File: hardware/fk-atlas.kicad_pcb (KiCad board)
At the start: 4 copper layers, 88.4 x 80.3 mm, 143 parts, among them J1 CONN_02x05_SWD, J10 CONN_01x04, J2 MICRO-USB-VERT-TOP, J201 CONN_01X02, J3 CONN_01x02, J301 CONN_01X02, J4 CONN_01x03_SERIAL, J401 CONN_01X02, J5 CONN_01x05, J501 CONN_01X02, J6 CONN_01x04, J601 CONN_01X02, J7 CONN_01x05, J8 CONN_01x02, J9 MICRO-USB-HORIZ-BOTTOM, M1 MOUNT_HOLE, M2 MOUNT_HOLE, M3 MOUNT_HOLE, M4 MOUNT_HOLE, M5 FIDUCIAL, M6 FIDUCIAL, M7 FIDUCIAL, P2 ATLAS_EC_PROBE, P3 ATLAS_RTD_PROBE, P4 ATLAS_PH_PROBE, P5 ATLAS_DO_PROBE, P6 ATLAS_ORP_PROBE, Q4 2N7002LT1G, SW1 SPNO, U1 S25FL116K0XMFI041, U2 ATSAMD21G18A-AU, U201 ADM3260, U202 ATLAS_EC, U3 MCP1700T-3302E/MB, U301 ADM3260, U302 ATLAS_RTD, U4 TPS2052B, U401 ADM3260, U402 ATLAS_PH, U5 SK6812, U501 ADM3260, U502 ATLAS_DO, U601 ADM3260, U602 ATLAS_ORP, Y1 FC-135

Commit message: Finished DRC check, no errors
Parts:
- added C22: 10uF, conservify:CAP-0603, F.Cu at (132.6, 119.0)
- added C23: 10uF, conservify:CAP-0603, F.Cu at (134.1, 119.0)
- added C24: 100nF, conservify:CAP-0603, F.Cu at (125.5, 132.2)
- added G***: LOGO, conservify:LOGO_CONSERVIFY_TEXT_NEGATIVE_4000, F.Cu at (136.0, 80.3)
- added G***: LOGO, conservify:LOGO_FK_NEGATIVE_2500, F.Cu at (141.1, 82.4)
- added G***: LOGO, conservify:LOGO_OSH_NEGATIVE_3000, F.Cu at (145.3, 135.0)
- J10: footprint conservify:Molex_CLIK-Mate_502382-0470_1x04_P1.25mm_Vertical -> conservify:BM04B-SRSS-TB
- R13, R14: value ? -> 100K
- moved R14 47.5 mm to (141.9, 124.2), turned to 270 degrees
- moved C606 6.17 mm to (187.2, 132.6), turned to 90 degrees
- moved C506 6.10 mm to (187.3, 116.7), turned to 90 degrees
- moved C18 4.85 mm to (143.4, 124.2)
- moved R12 4.32 mm to (137.0, 126.2)
- moved C19 3.89 mm to (140.5, 124.2)
- moved J10 3.19 mm to (126.6, 127.3)
- moved C406 1.05 mm to (187.5, 100.8)
- moved C306 0.79 mm to (187.5, 85.3), turned to 90 degrees
- moved C206 0.57 mm to (187.5, 68.8)
- moved R7 0.28 mm to (138.9, 124.2)
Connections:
- J10 pad 1: Net-(J10-Pad1) -> GND
- J10 pad 2: Net-(J10-Pad2) -> 3V3
- J10 pad 3: Net-(J10-Pad3) -> /SDA2
- J10 pad 4: Net-(J10-Pad4) -> /SCL2
- J5 pad 3: VIN -> Net-(J5-Pad3)
- J7 pad 3: VIN -> Net-(J7-Pad3)
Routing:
- net VCC: track 29.4 -> 50.0 mm, vias 6 -> 21
- net /PERIPH_3V3: track 40.9 -> 59.8 mm
- net /isolated_atlas2/ISO_SDA: track 20.5 -> 37.5 mm
- net /isolated_atlas3/ISO_SDA: track 20.4 -> 37.3 mm
- net Net-(J301-Pad2): track 11.8 -> 24.1 mm
- net /isolated_atlas1/ISO_VCC: track 12.5 -> 22.0 mm, vias 2 -> 4
- net /isolated_atlas2/ISO_VCC: track 13.0 -> 20.5 mm, vias 3 -> 4
- net /isolated_atlas0/ISO_VCC: track 14.3 -> 21.0 mm
- net GND: track 107.0 -> 100.7 mm, vias 61 -> 77
- net Net-(R12-Pad1): track 3.88 -> 9.76 mm, vias 0 -> 2
- net Net-(J401-Pad2): track 9.52 -> 15.0 mm
- net /isolated_atlas3/ISO_GND: track 7.87 -> 12.8 mm, vias 3 -> 8
- net /isolated_atlas2/ISO_SCL: track 20.3 -> 24.4 mm
- net /isolated_atlas3/ISO_SCL: track 20.3 -> 24.4 mm
- net 3V3: track 36.5 -> 32.4 mm, vias 25 -> 34
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- added copper zone on PWR, net /isolated_atlas3/ISO_VCC
- removed copper zone on PWR, net VIN

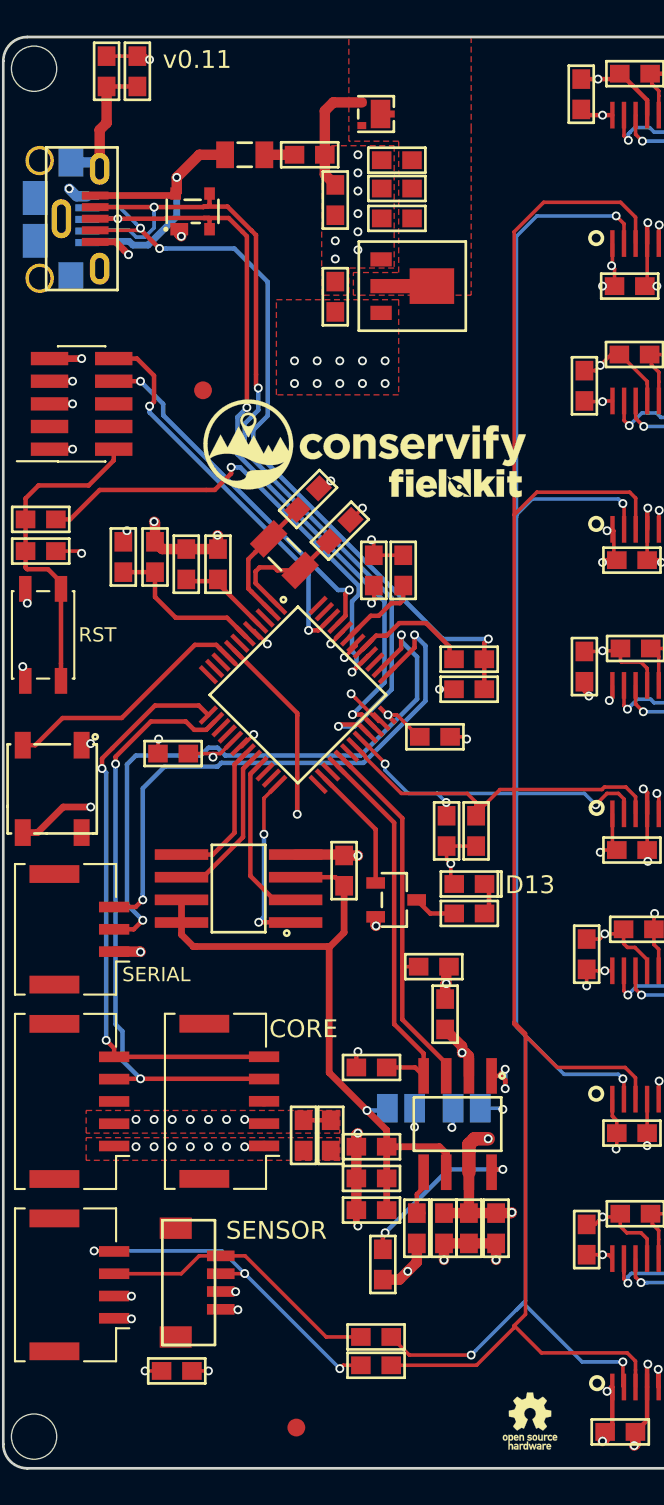
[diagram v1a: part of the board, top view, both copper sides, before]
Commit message: Added a power indicator LED, finished touching up traces and added logos, markings back in
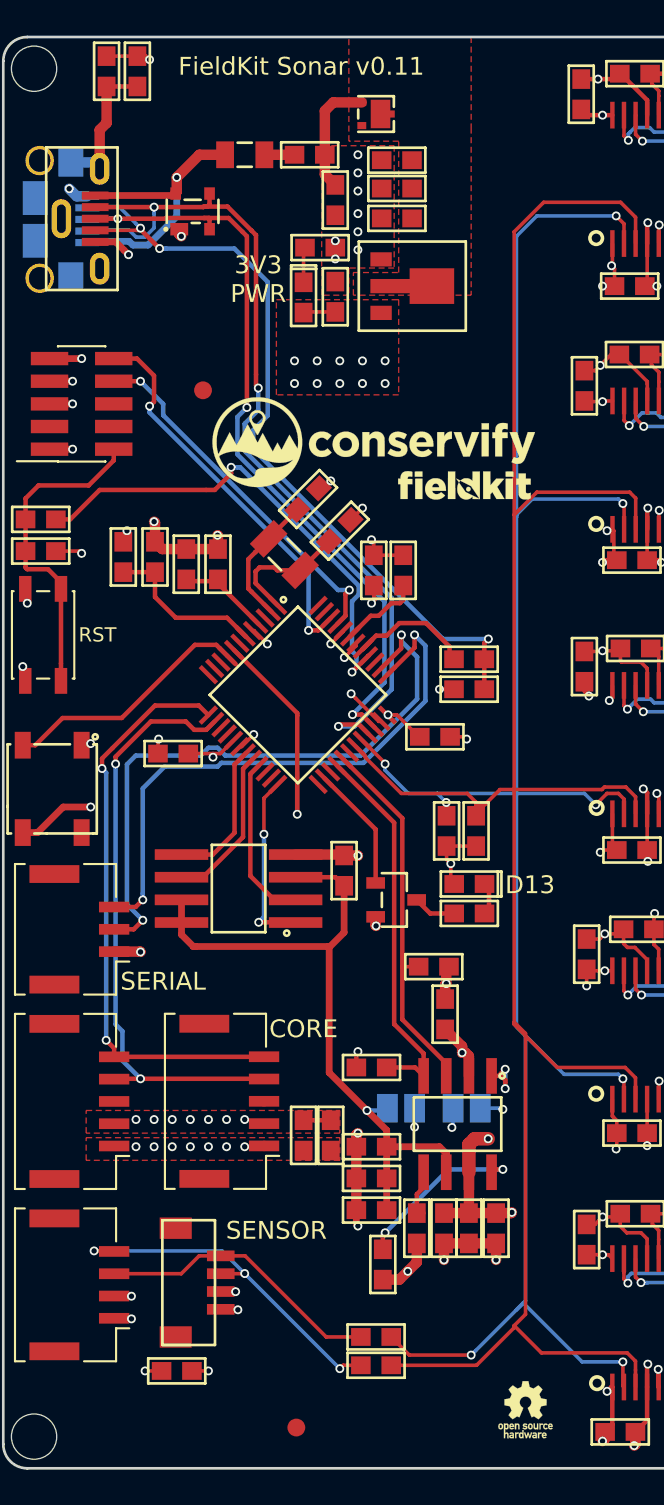
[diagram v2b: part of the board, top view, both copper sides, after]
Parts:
- added D1: Green, conservify:LED-0603, F.Cu at (132.6, 72.0)
- added R17: 2K2, conservify:RES-0603, F.Cu at (133.5, 69.2)
- moved G*** 0.68 mm to (145.0, 134.4)
- moved G*** 0.52 mm to (136.5, 80.1)
- moved G*** 0.52 mm to (141.6, 82.5)
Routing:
- net Net-(D1-Pad1): track 0.00 -> 1.98 mm
- net 3V3: track 32.4 -> 34.2 mm
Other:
- board text added: "3V3 PWR"
- board text added: "FieldKit Sonar v0.11"
- board text removed: "v0.11"

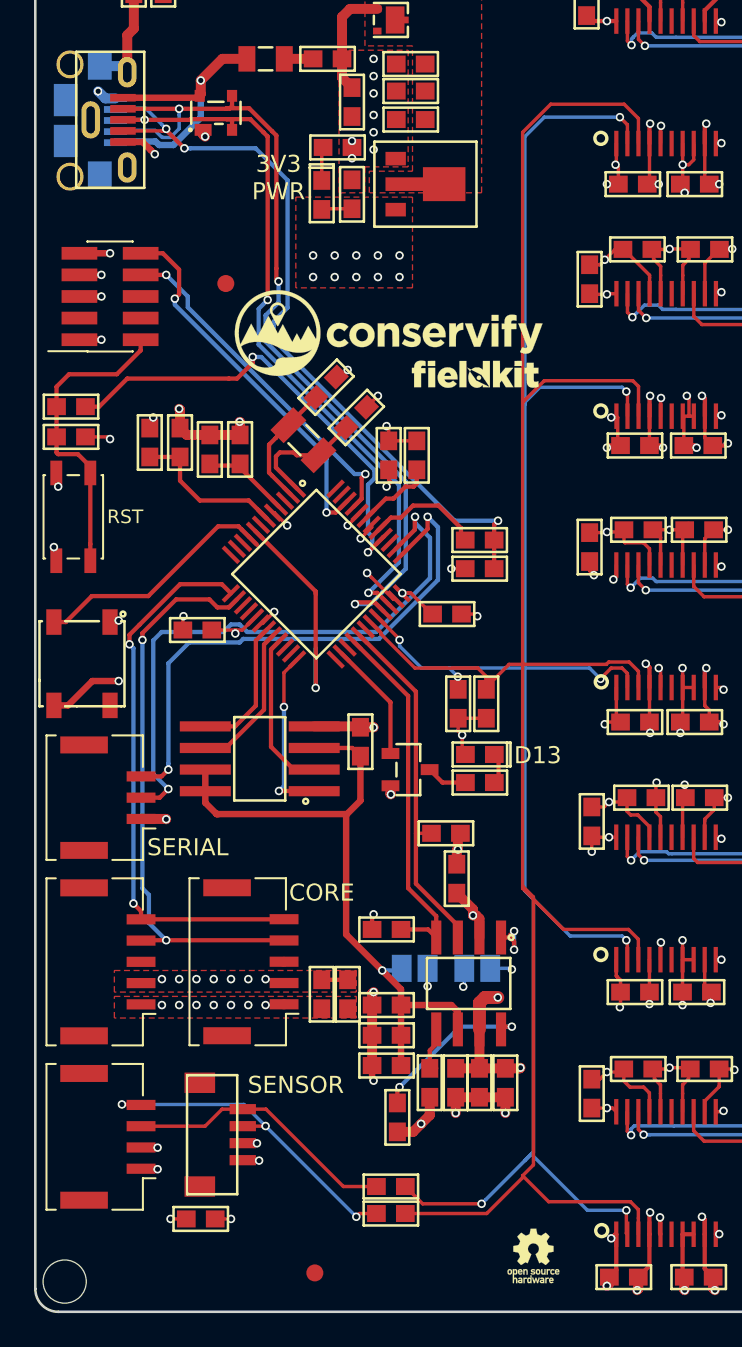
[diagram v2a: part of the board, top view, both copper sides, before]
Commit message: Added pull up resistors and a debounce cap for the reset button
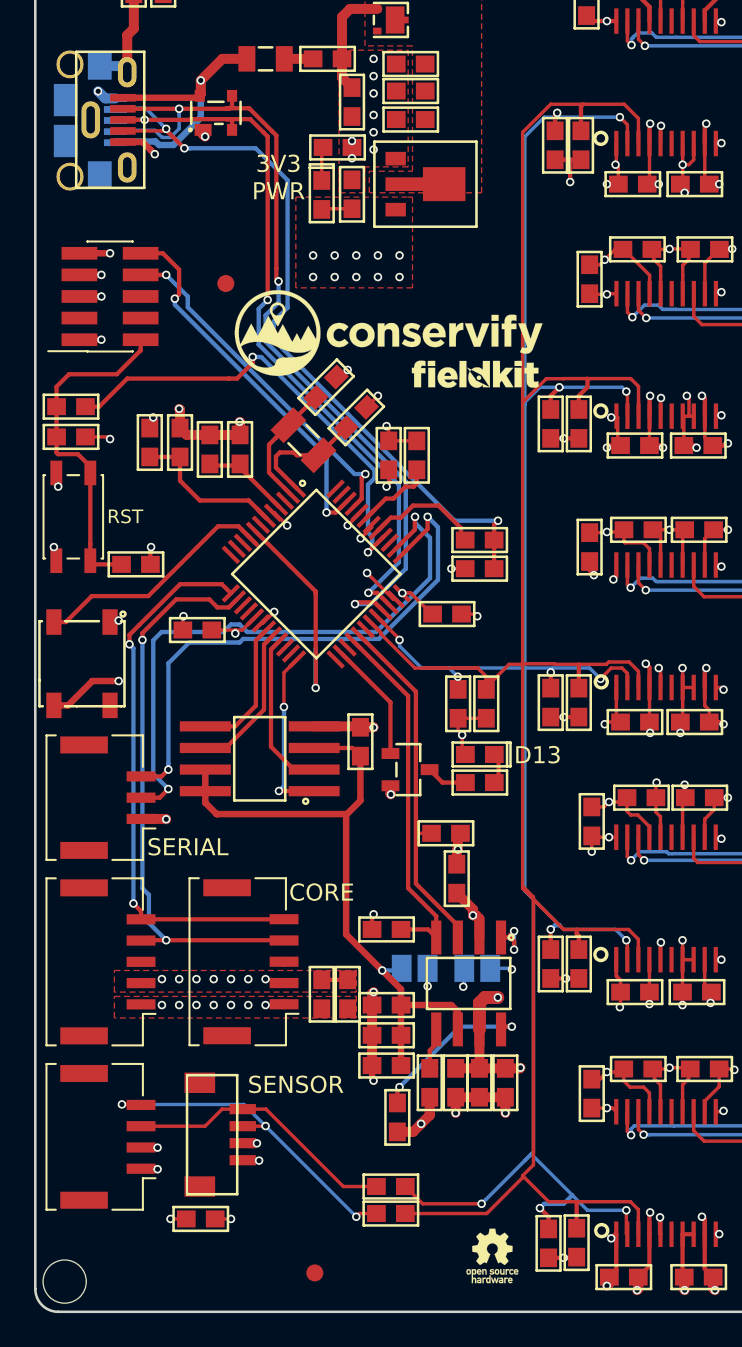
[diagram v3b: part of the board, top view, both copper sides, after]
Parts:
- added C25: 100nF, conservify:CAP-0603, F.Cu at (121.7, 93.7)
- added R18: 4.7K, conservify:RES-0603, F.Cu at (147.7, 117.2)
- added R19: 4.7K, conservify:RES-0603, F.Cu at (146.1, 117.2)
- added R20: 4.7K, conservify:RES-0603, F.Cu at (147.8, 69.1)
- added R21: 4.7K, conservify:RES-0603, F.Cu at (146.3, 69.1)
- added R22: 4.7K, conservify:RES-0603, F.Cu at (146.1, 85.5)
- added R23: 4.7K, conservify:RES-0603, F.Cu at (147.7, 85.5)
- added R24: 4.7K, conservify:RES-0603, F.Cu at (146.1, 101.9)
- added R25: 4.7K, conservify:RES-0603, F.Cu at (147.7, 101.9)
- added R26: 4.7K, conservify:RES-0603, F.Cu at (145.9, 133.6)
- added R27: 4.7K, conservify:RES-0603, F.Cu at (147.6, 133.6)
- moved G*** 2.41 mm to (142.6, 134.4)
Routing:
- net /SCL1: track 121.3 -> 130.9 mm, vias 8 -> 13
- net VCC: track 50.0 -> 59.5 mm, vias 21 -> 26
- net /SDA1: track 126.1 -> 134.1 mm
- net /RST: track 18.2 -> 20.1 mm
- net GND: track 100.7 -> 101.7 mm, vias 77 -> 78

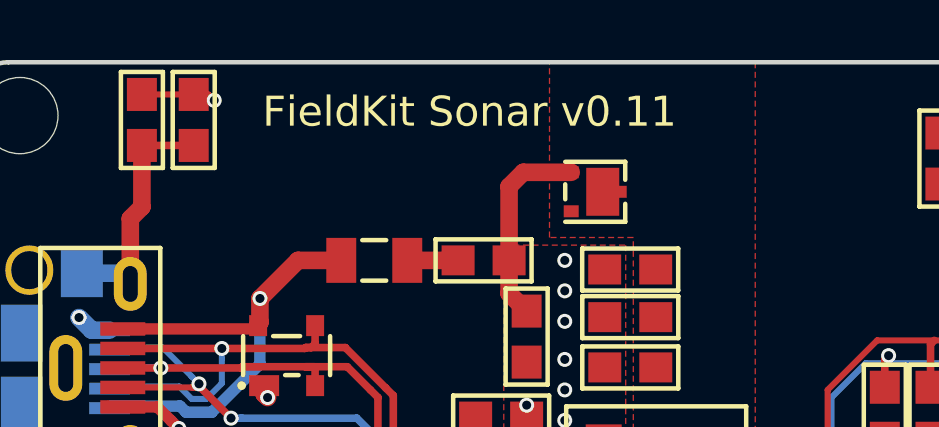
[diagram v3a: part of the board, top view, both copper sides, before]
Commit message: Fix board name on silk.
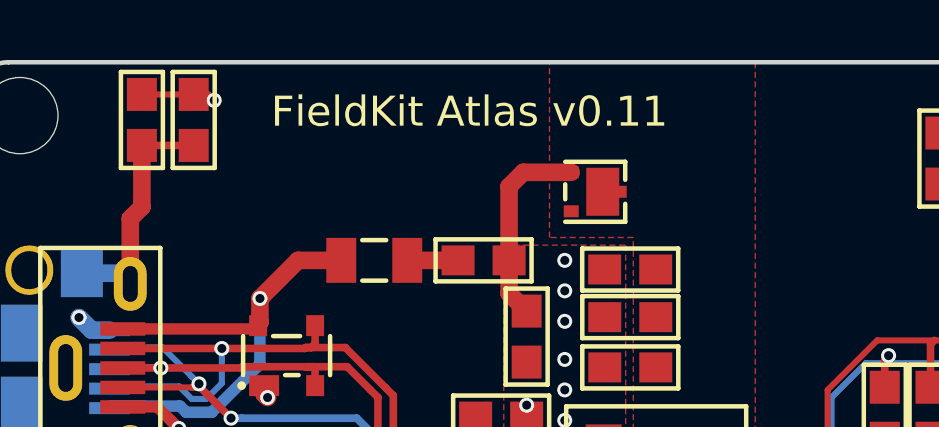
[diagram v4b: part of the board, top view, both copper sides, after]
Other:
- board text added: "FieldKit Atlas v0.11"
- board text removed: "FieldKit Sonar v0.11"
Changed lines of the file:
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@@
-(kicad_pcb (version 20171130) (host pcbnew "(5.0.0)")
+(kicad_pcb (version 20171130) (host pcbnew 5.0.1-33cea8e~67~ubuntu18.04.1)
   (general
     (thickness 1.6)
@@
     (effects (font (size 1.5 1.5) (thickness 0.25)))
   )
-  (gr_text "FieldKit Sonar v0.11" (at 132.461 59.055) (layer F.SilkS)
+  (gr_text "FieldKit Atlas v0.11" (at 132.461 59.055) (layer F.SilkS)
     (effects (font (size 1 1) (thickness 0.2)))
   )

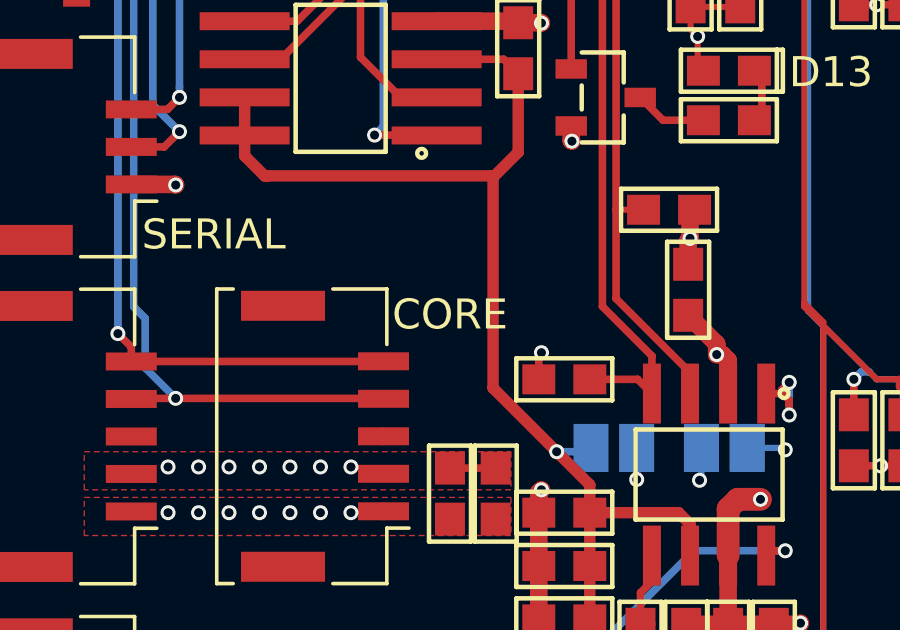
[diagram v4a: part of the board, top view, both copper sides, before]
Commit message: Generated panelized version of v0.11, including gerbers
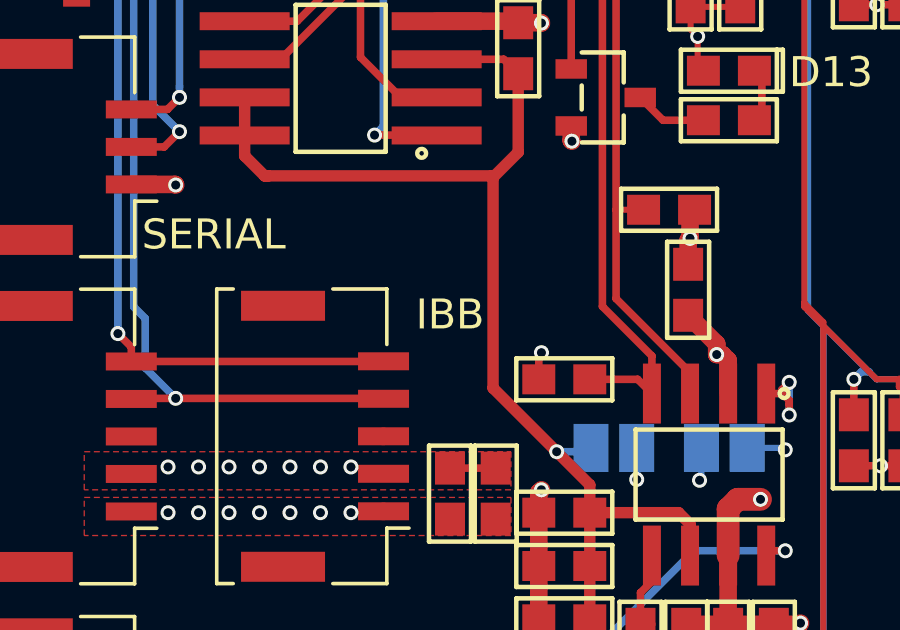
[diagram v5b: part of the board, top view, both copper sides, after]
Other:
- board text added: "IBB"
- board text removed: "CORE"
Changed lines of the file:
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@@
-(kicad_pcb (version 20171130) (host pcbnew 5.0.1-33cea8e~67~ubuntu18.04.1)
+(kicad_pcb (version 20171130) (host pcbnew "(5.0.0)")
   (general
     (thickness 1.6)
@@
       (drillshape 0)
       (scaleselection 1)
-      (outputdirectory "gerbers"))
+      (outputdirectory "gerbers/v0.11/"))
   )
   (net 0 "")
@@
     (effects (font (size 0.8 0.8) (thickness 0.2)))
   )
-  (gr_text CORE (at 132.588 113.03) (layer F.SilkS)
+  (gr_text IBB (at 132.588 113.03) (layer F.SilkS)
     (effects (font (size 1 1) (thickness 0.2)))
   )
